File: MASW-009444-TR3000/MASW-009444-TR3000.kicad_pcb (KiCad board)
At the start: 2 copper layers, 1 x 13.7 mm, 2 parts

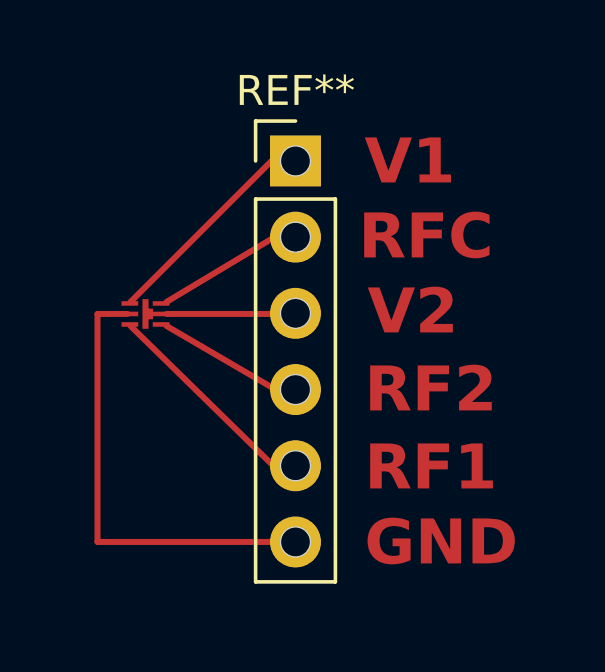
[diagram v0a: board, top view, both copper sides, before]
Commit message: added switches
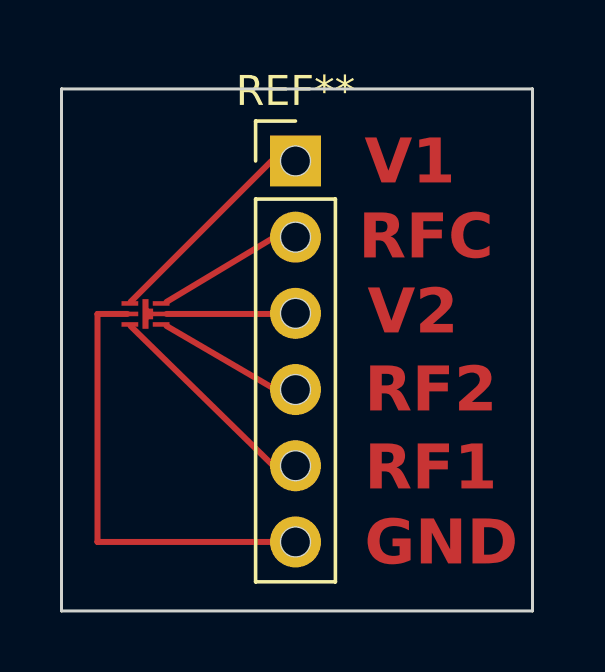
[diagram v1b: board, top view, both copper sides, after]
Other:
- board size 1 x 13.7 mm -> 15.7 x 17.4 mm
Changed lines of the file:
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@@
       (outputformat 1)
       (mirror false)
-      (drillshape 1)
+      (drillshape 0)
       (scaleselection 1)
-      (outputdirectory "")
+      (outputdirectory "/Volumes/MIC FD/RF/MASW-009444/")
     )
   )
@@
   (gr_circle (center 142.8 87.46) (end 143.3 87.46)
     (stroke (width 0.01) (type default)) (fill none) (layer "Edge.Cuts"))
+  (gr_rect (start 135 74.9) (end 150.7 92.3)
+    (stroke (width 0.1) (type default)) (fill none) (layer "Edge.Cuts"))
   (gr_circle (center 142.8 77.3) (end 143.3 77.3)
     (stroke (width 0.01) (type default)) (fill none) (layer "Edge.Cuts"))
